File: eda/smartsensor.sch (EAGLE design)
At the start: 44 parts, among them U1 ISL83491SOIC, U2 ATTINY1634, U3 3.3V

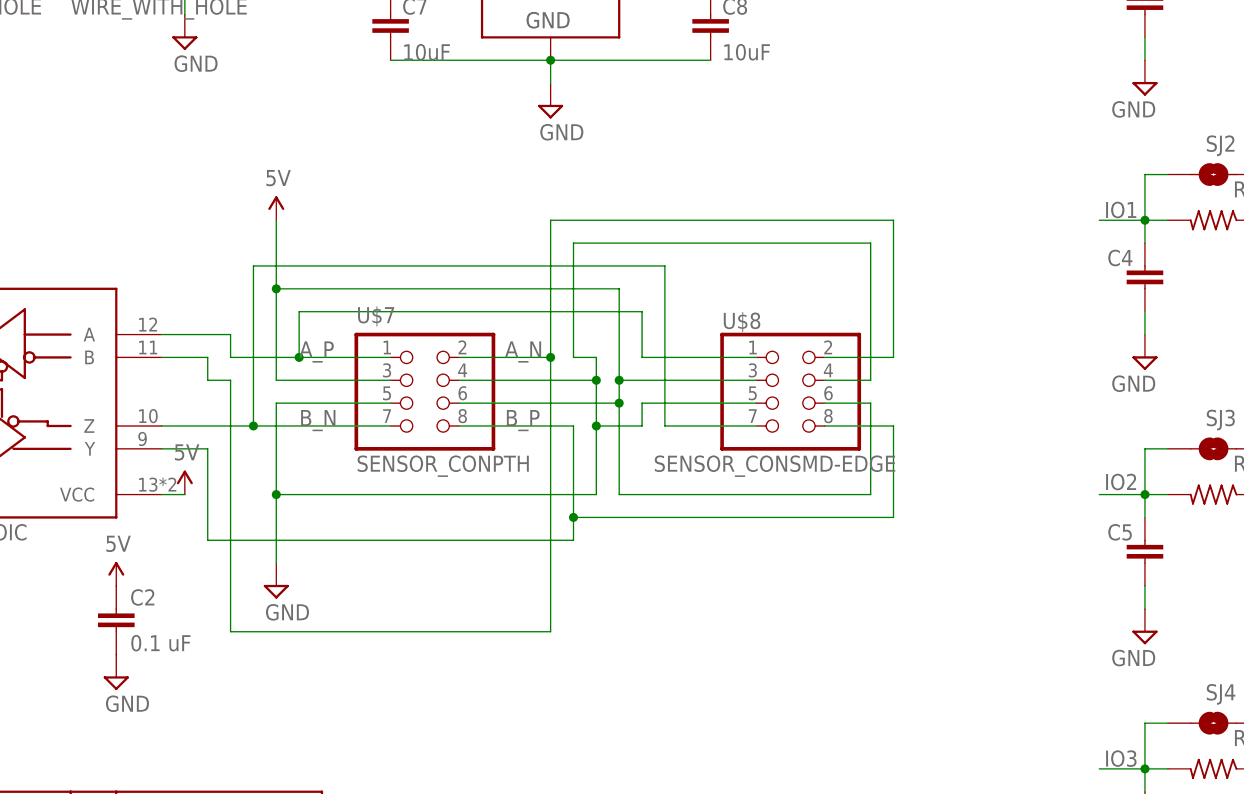
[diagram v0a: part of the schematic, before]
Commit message: Replaced 2x4 connectors with 2x5's.
On smartsensor, smartsensorPowered, smartsensor_powered_jig, and team_flag.
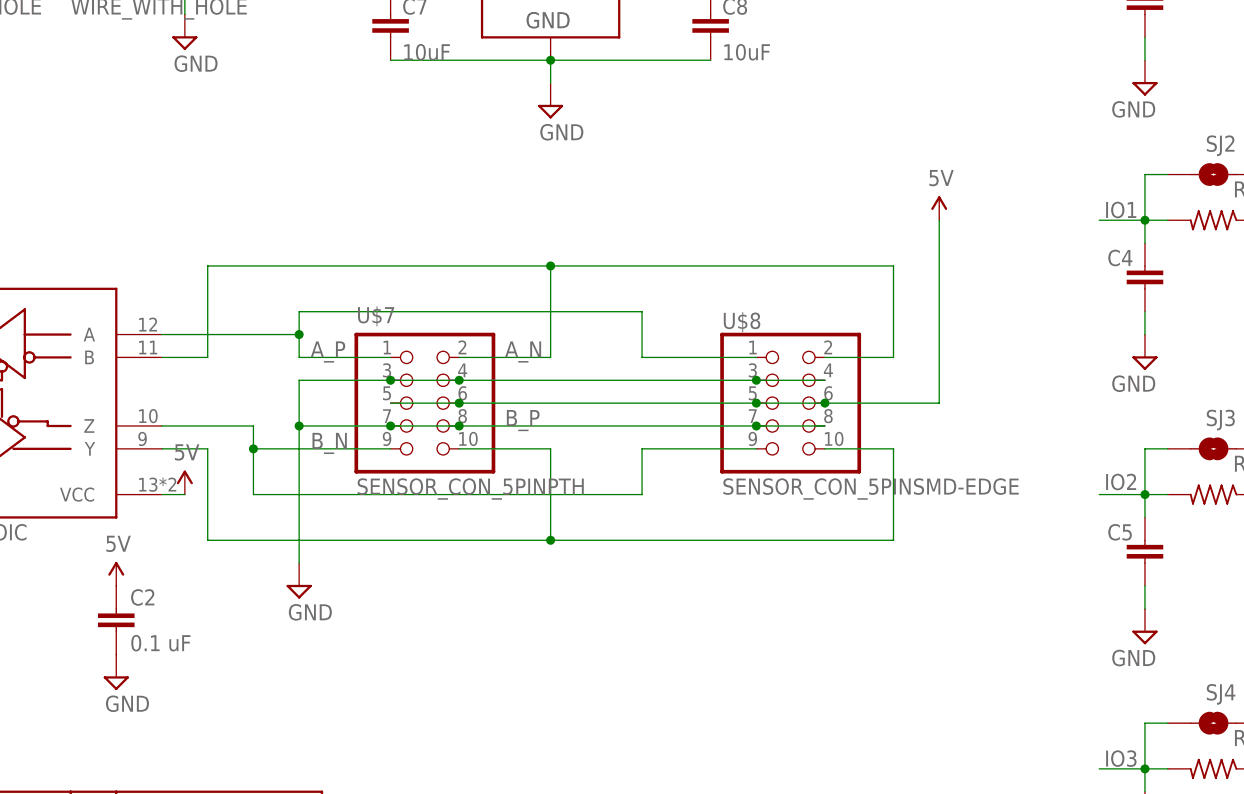
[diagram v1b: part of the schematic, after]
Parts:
- U$7: value SENSOR_CONPTH -> SENSOR_CON_5PINPTH; device pie:SENSOR_CONPTH -> pie:SENSOR_CON_5PINPTH
- U$8: value SENSOR_CONSMD-EDGE -> SENSOR_CON_5PINSMD-EDGE; device pie:SENSOR_CONSMD-EDGE -> pie:SENSOR_CON_5PINSMD-EDGE
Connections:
- net 5V: now also U$7.5, U$8.5; no longer U$7.3, U$8.3
- net B_N: now also U$7.9, U$8.9; no longer U$7.7, U$8.7
- net B_P: now also U$7.10, U$8.10; no longer U$7.8, U$8.8
- net GND: now also U$7.3, U$7.7, U$7.8, U$8.3, U$8.7, U$8.8; no longer U$7.5, U$8.5
